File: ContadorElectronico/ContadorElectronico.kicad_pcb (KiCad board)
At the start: 2 copper layers, 98 x 52 mm, 33 parts, among them J1 Conn_01x01_Pin, J2 Conn_01x01_Pin, J3 Conn_01x01_Pin, J4 Conn_01x01_Pin, J5 Conn_01x01_Pin, J6 Conn_01x01_Pin, J7 INPUT, J8 POWER, SW1 MODE, SW2 INC, SW3 DEC, U1 LM358, U3 4N35, U4 4N35

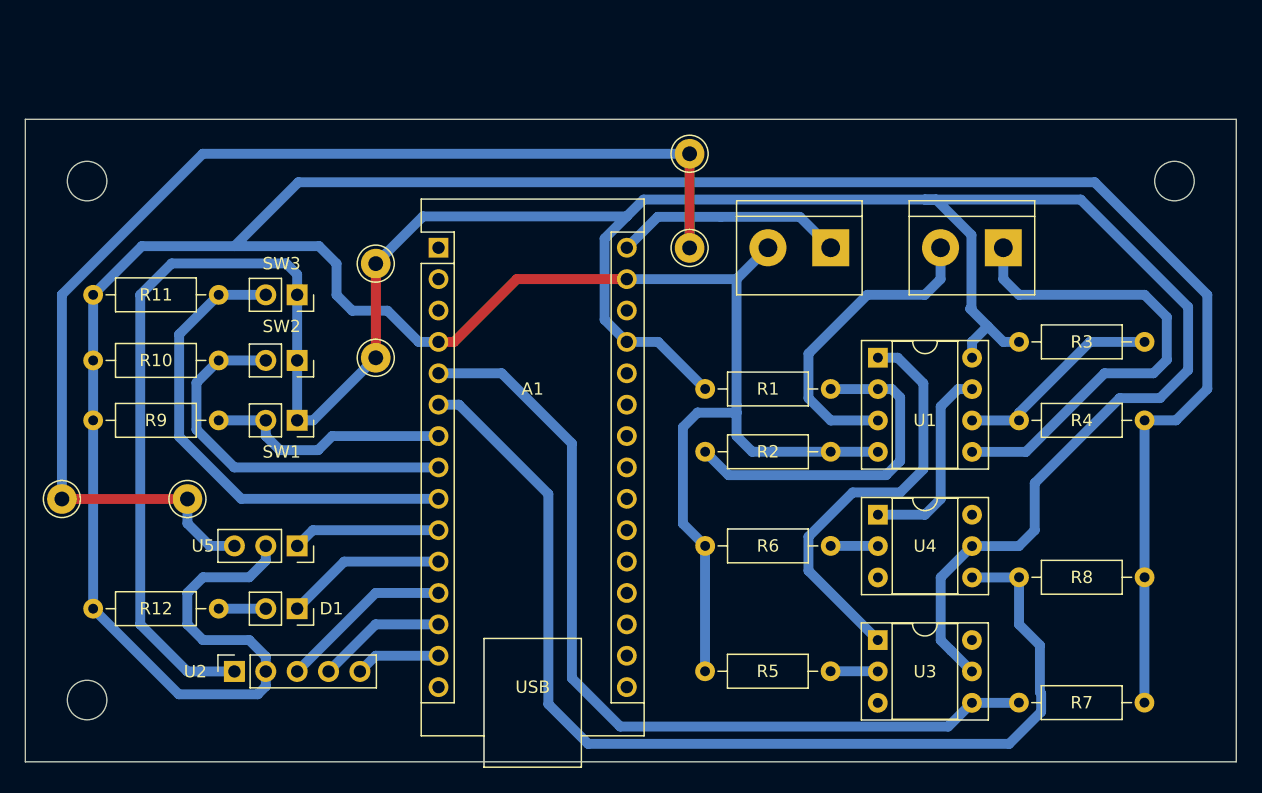
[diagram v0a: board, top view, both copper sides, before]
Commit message: Agregado plano de tierra
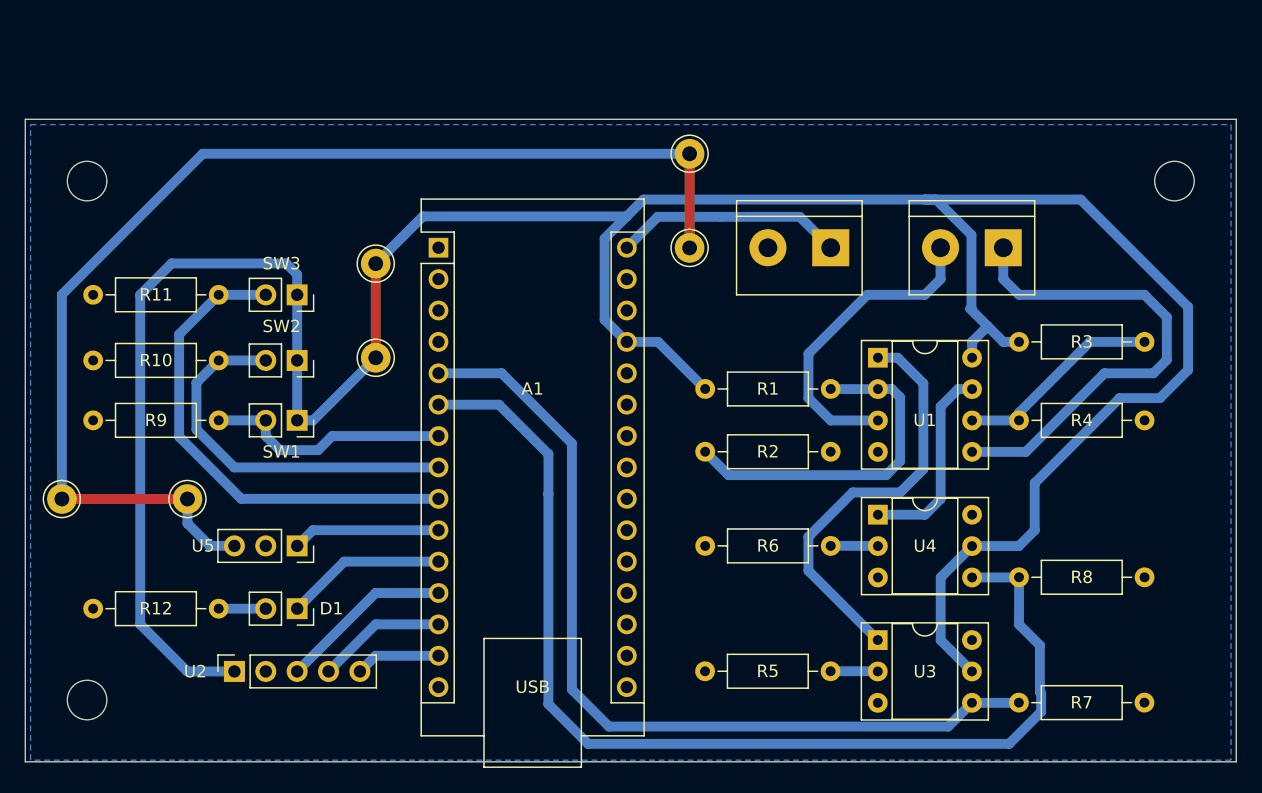
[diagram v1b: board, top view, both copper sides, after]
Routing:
- net GND: track 298.9 -> 0.00 mm
- net /RESET: track 86.6 -> 88.5 mm
- net /COUNT: track 70.7 -> 71.3 mm
- added copper zone on B.Cu, net GND

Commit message: PCB design with 3 pin bornier
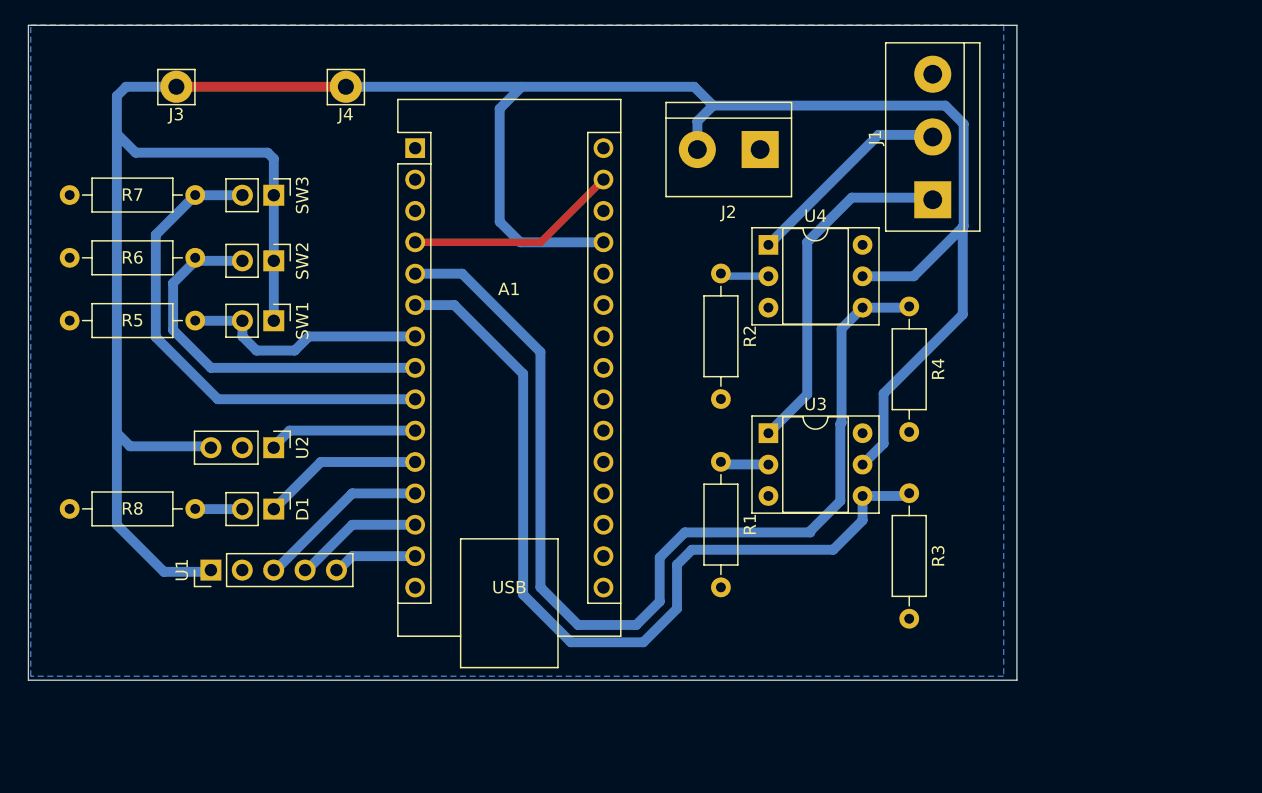
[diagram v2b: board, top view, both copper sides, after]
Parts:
- removed J5, J6: Conn_01x01_Pin, Connector_Pin:Pin_D1.0mm_L10.0mm_LooseFit
- removed J7: INPUT, TerminalBlock:TerminalBlock_bornier-2_P5.08mm
- removed J8: POWER, TerminalBlock:TerminalBlock_bornier-2_P5.08mm
- removed R10, R11, R9: 1K, Resistor_THT:R_Axial_DIN0207_L6.3mm_D2.5mm_P10.16mm_Horizontal
- removed R12: 220, Resistor_THT:R_Axial_DIN0207_L6.3mm_D2.5mm_P10.16mm_Horizontal
- removed REF** (x3): MountingHole_3.2mm_M3, MountingHole:MountingHole_3.2mm_M3
- removed U5: ~, Connector_PinSocket_2.54mm:PinSocket_1x03_P2.54mm_Vertical
- D1, SW1, SW2, SW3: footprint Connector_PinSocket_2.54mm:PinSocket_1x02_P2.54mm_Vertical -> Connector_PinHeader_2.54mm:PinHeader_1x02_P2.54mm_Vertical
- J1: value Conn_01x01_Pin -> INPUT; footprint Connector_Pin:Pin_D1.0mm_L10.0mm_LooseFit -> TerminalBlock:TerminalBlock_bornier-3_P5.08mm
- J2: value Conn_01x01_Pin -> POWER; footprint Connector_Pin:Pin_D1.0mm_L10.0mm_LooseFit -> TerminalBlock:TerminalBlock_bornier-2_P5.08mm
- J3, J4: footprint Connector_Pin:Pin_D1.0mm_L10.0mm_LooseFit -> Connector_Pin:Pin_D1.3mm_L11.3mm_W2.8mm_Flat
- R2, R4: value 100 -> 10k
- R5, R6: value 220 -> 1K
- R7: value 10k -> 1K
- R8: value 10k -> 220
- U1: value LM358 -> ~; footprint Package_DIP:DIP-8_W7.62mm_Socket -> Connector_PinHeader_2.54mm:PinHeader_1x05_P2.54mm_Vertical
- U2: footprint Connector_PinSocket_2.54mm:PinSocket_1x05_P2.54mm_Vertical -> Connector_PinHeader_2.54mm:PinHeader_1x03_P2.54mm_Vertical
- moved R7 78.3 mm to (63.5, 38.7), turned to 180 degrees
- moved J1 74.5 mm to (123.2, 39.1), turned to 90 degrees
- moved R8 66.9 mm to (63.5, 64.1), turned to 180 degrees
- moved R5 58.7 mm to (63.5, 48.9)
- moved U1 56.7 mm to (64.8, 69.1), turned to 90 degrees
- moved R6 56.5 mm to (63.5, 43.8)
- moved J2 54.3 mm to (109.2, 35.1), turned to 180 degrees
- moved J3 41.9 mm to (62.0, 30.0)
- moved J4 30.7 mm to (75.7, 30.0)
- moved U4 23.6 mm to (109.9, 42.8)
- moved U3 18.9 mm to (109.9, 58.0)
- moved U2 18.4 mm to (69.8, 59.2), turned to -90 degrees
- moved R3 15.1 mm to (121.3, 62.9), turned to -90 degrees
- moved R2 14.5 mm to (106.0, 45.1), turned to -90 degrees
- moved R4 12.8 mm to (121.3, 47.8), turned to -90 degrees
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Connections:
- A1 pad 30: +9V -> unconnected-(A1-VIN-Pad30)
- A1 pad 5: /COUNT -> /RESET
- A1 pad 6: /RESET -> /COUNT
- J1 pad 1: +9V -> /COUNT_IN
- J2 pad 1: +9V -> GND
- J3 pad 1: +9V -> +5V
- J4 pad 1: +9V -> +5V
- R1 pad 1: +5V -> Net-(R1-Pad1)
- R1 pad 2: Net-(U1A--) -> GND
- R2 pad 1: Net-(U1A--) -> Net-(R2-Pad1)
- R3 pad 1: +5V -> /COUNT
- R3 pad 2: Net-(U1B--) -> GND
- R4 pad 1: Net-(U1B--) -> /RESET
- R5 pad 1: Net-(R5-Pad1) -> /MODE
- R6 pad 1: Net-(R6-Pad1) -> /INC
- R7 pad 1: /COUNT -> /DEC
- R8 pad 1: /RESET -> Net-(D1-A)
- U1 pad 1: Net-(U1-Pad1) -> +5V
- U1 pad 2: Net-(U1A--) -> GND
- U1 pad 3: /COUNT_IN -> Net-(A1-D9)
- U1 pad 4: GND -> Net-(A1-D10)
- U1 pad 5: /RESET_IN -> Net-(A1-D11)
- U2 pad 1: +5V -> /RELAY
- U2 pad 3: Net-(A1-D9) -> +5V
- U3 pad 1: Net-(U1-Pad1) -> /COUNT_IN
- U3 pad 2: Net-(R5-Pad1) -> Net-(R1-Pad1)
- U4 pad 1: Net-(U1-Pad7) -> /RESET_IN
- U4 pad 2: Net-(R6-Pad1) -> Net-(R2-Pad1)
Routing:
- net +9V: track 117.5 -> 0.00 mm
- net Net-(U1-Pad1): track 33.7 -> 0.00 mm
- net Net-(U1A--): track 28.1 -> 0.00 mm
- net /RESET_IN: track 39.4 -> 17.0 mm
- net GND: track 0.00 -> 17.3 mm
- net Net-(U1B--): track 17.0 -> 0.00 mm
- net Net-(U1-Pad7): track 16.2 -> 0.00 mm
- net +5V: track 231.0 -> 215.3 mm
- net /RESET: track 88.5 -> 83.9 mm
- net Net-(R6-Pad1): track 3.83 -> 0.00 mm
- net Net-(R5-Pad1): track 3.83 -> 0.00 mm
- net Net-(R2-Pad1): track 0.00 -> 3.83 mm
- net Net-(R1-Pad1): track 0.00 -> 3.83 mm
- net /COUNT_IN: track 25.7 -> 28.4 mm
- net /COUNT: track 71.3 -> 69.9 mm
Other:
- board size 98 x 52 mm -> 80 x 53 mm

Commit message: 2 Pin Bornier for inputs
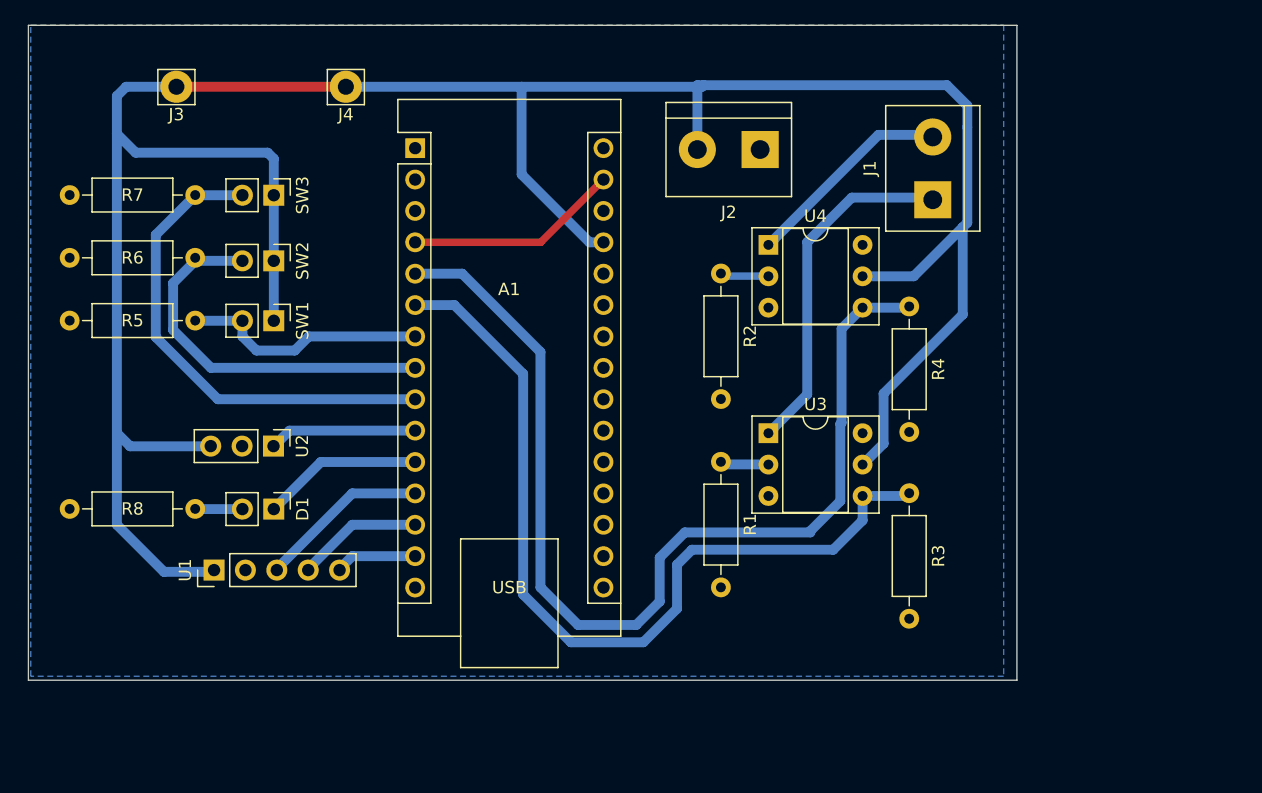
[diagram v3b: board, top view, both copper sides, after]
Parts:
- J1: footprint TerminalBlock:TerminalBlock_bornier-3_P5.08mm -> TerminalBlock:TerminalBlock_bornier-2_P5.08mm
- moved U1 0.25 mm to (65.0, 69.1)
- moved U2 0.13 mm to (69.8, 59.1)
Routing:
- net +5V: track 215.3 -> 213.5 mm
